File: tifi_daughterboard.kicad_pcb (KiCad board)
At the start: 2 copper layers, 57.4 x 32.3 mm, 19 parts, among them J1 SSW-110-23-F-D, J2 SSW-110-23-F-D, J3 SM04B-SRSS-TB(LF)(SN), J4 SSW-103-02-T-S-RA, Q1 BSS138LT1G, U1 SGP40-D-R4, U2 SHT40-AD1B-R3

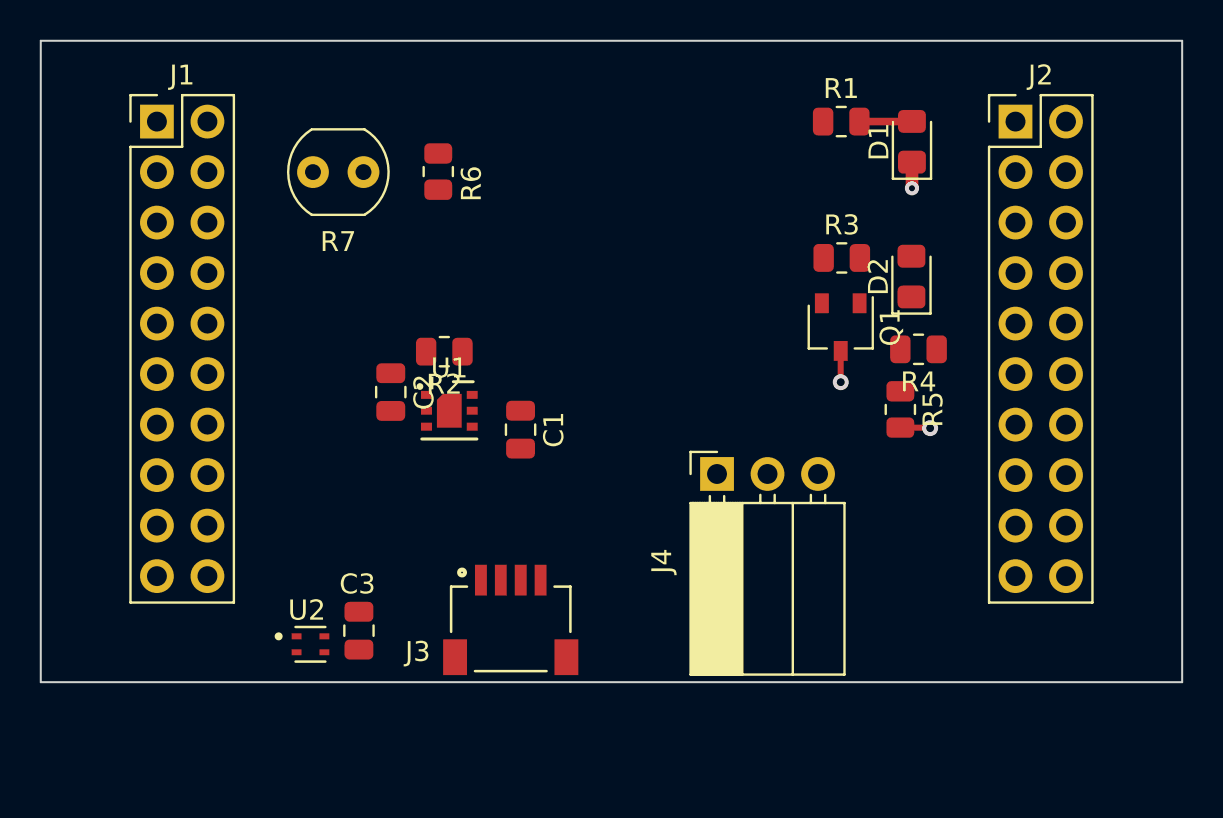
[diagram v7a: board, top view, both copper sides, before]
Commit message: Route I2C connections.
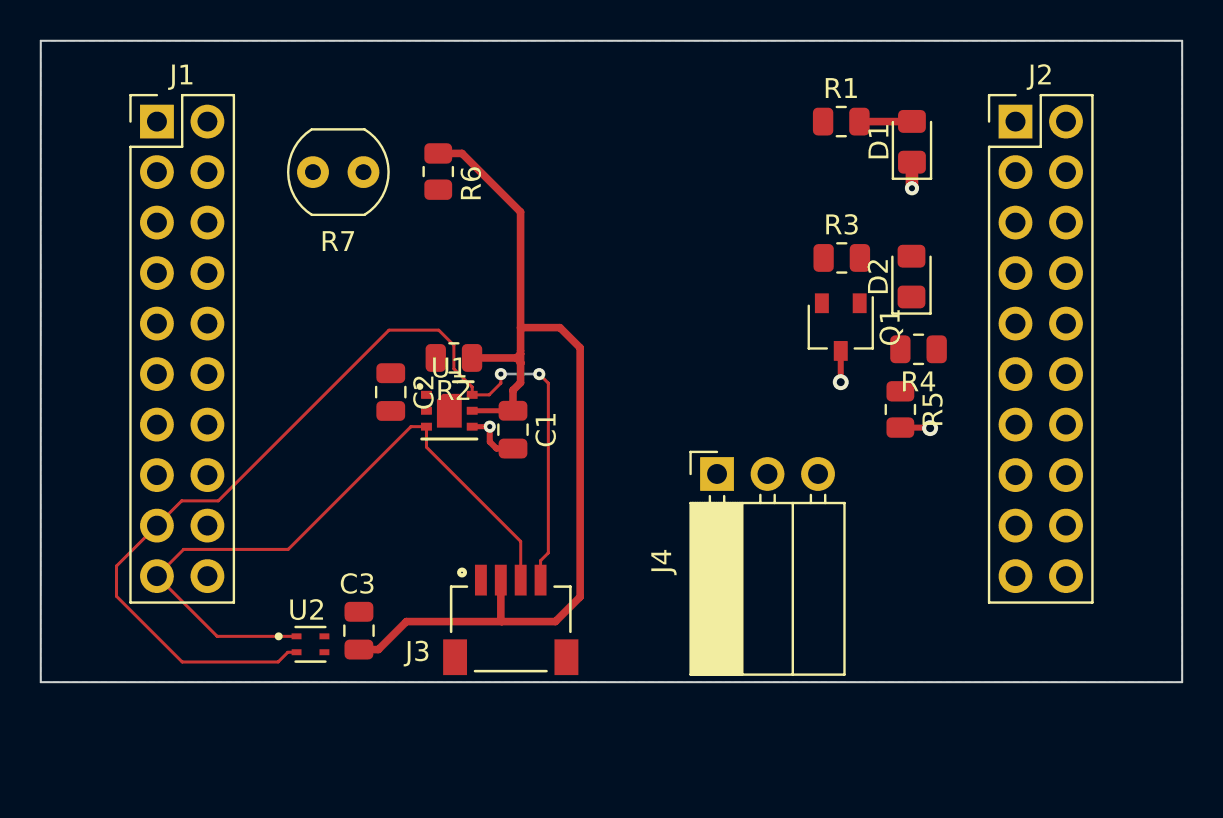
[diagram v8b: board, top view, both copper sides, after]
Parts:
- moved R2 0.58 mm to (136.9, 85.5)
- moved C1 0.38 mm to (139.8, 89.2)
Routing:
- net I2C_SCL: track 0.00 -> 52.0 mm, vias 0 -> 2
- net +3.3V: track 0.00 -> 51.0 mm
- net I2C_SDA: track 0.00 -> 34.6 mm
- net GND: track 4.39 -> 7.35 mm, vias 3 -> 4
- added copper zone on B.Cu, net GND
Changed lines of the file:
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@@
     )
     (pad_to_mask_clearance 0)
+    (grid_origin 140.3858 87.4268)
     (pcbplotparams
       (layerselection 0x00010fc_ffffffff)
@@
   )
   (footprint "Resistor_SMD:R_0805_2012Metric" (layer "F.Cu")
-    (at 136.3726 85.2322 180)
+    (at 136.8552 85.5472 180)
     (descr "Resistor SMD 0805 (2012 Metric), square (rectangular) end terminal, IPC_7351 nominal, (Body size source: IPC-SM-782 page 72, https://www.pcb-3d.com/wordpress/wp-content/uploads/ipc-sm-782a_amendment_1_and_2.pdf), generated with kicad-footprint-generator")
     (tags "resistor")
@@
   )
   (footprint "Capacitor_SMD:C_0805_2012Metric" (layer "F.Cu")
-    (at 140.208 89.154 -90)
+    (at 139.827 89.154 -90)
     (descr "Capacitor SMD 0805 (2012 Metric), square (rectangular) end terminal, IPC_7351 nominal, (Body size source: IPC-SM-782 page 76, https://www.pcb-3d.com/wordpress/wp-content/uploads/ipc-sm-782a_amendment_1_and_2.pdf, https://docs.google.com/spreadsheets/d/1BsfQQcO9C6DZCsRaXUlFlo91Tg2WpOkGARC1WS5S8t0/edit?usp=sharing), generated with kicad-footprint-generator")
     (tags "capacitor")
@@
   )
   (gr_rect (start 116.078 69.596) (end 173.482 101.854) (layer "Edge.Cuts") (width 0.1016) (fill none))
+  (segment (start 139.2682 98.806) (end 134.4676 98.806) (width 0.381) (layer "F.Cu") (net 1))
+  (segment (start 141.9606 98.806) (end 139.2682 98.806) (width 0.381) (layer "F.Cu") (net 1))
+  (segment (start 139.2682 98.806) (end 139.215 98.7528) (width 0.381) (layer "F.Cu") (net 1))
+  (segment (start 136.0678 75.2621) (end 137.2635 75.2621) (width 0.381) (layer "F.Cu") (net 1))
+  (segment (start 139.215 98.7528) (end 139.215 96.7232) (width 0.381) (layer "F.Cu") (net 1))
+  (segment (start 143.2052 97.5614) (end 141.9606 98.806) (width 0.381) (layer "F.Cu") (net 1))
+  (segment (start 133.0604 100.2132) (end 132.08 100.2132) (width 0.381) (layer "F.Cu") (net 1))
+  (segment (start 140.208 78.2066) (end 140.208 84.0232) (width 0.381) (layer "F.Cu") (net 1))
+  (segment (start 140.208 86.7918) (end 139.827 87.1728) (width 0.381) (layer "F.Cu") (net 1))
+  (segment (start 140.208 84.0232) (end 142.1892 84.0232) (width 0.381) (layer "F.Cu") (net 1))
+  (segment (start 140.208 85.852) (end 140.208 85.7504) (width 0.381) (layer "F.Cu") (net 1))
+  (segment (start 139.827 87.1728) (end 139.827 88.204) (width 0.381) (layer "F.Cu") (net 1))
+  (segment (start 142.1892 84.0232) (end 143.2052 85.0392) (width 0.381) (layer "F.Cu") (net 1))
+  (segment (start 140.208 85.344) (end 140.208 85.852) (width 0.381) (layer "F.Cu") (net 1))
+  (segment (start 140.208 85.1916) (end 140.208 85.344) (width 0.381) (layer "F.Cu") (net 1))
+  (segment (start 137.2635 75.2621) (end 140.208 78.2066) (width 0.381) (layer "F.Cu") (net 1))
+  (segment (start 140.208 84.0232) (end 140.208 85.1916) (width 0.381) (layer "F.Cu") (net 1))
+  (segment (start 140.208 85.344) (end 140.0048 85.5472) (width 0.381) (layer "F.Cu") (net 1))
+  (segment (start 143.2052 85.0392) (end 143.2052 97.5614) (width 0.381) (layer "F.Cu") (net 1))
+  (segment (start 137.7766 88.204) (end 139.827 88.204) (width 0.254) (layer "F.Cu") (net 1))
+  (segment (start 140.208 85.852) (end 140.208 86.7918) (width 0.381) (layer "F.Cu") (net 1))
+  (segment (start 137.5645 85.5472) (end 140.0048 85.5472) (width 0.381) (layer "F.Cu") (net 1))
+  (segment (start 134.4676 98.806) (end 133.0604 100.2132) (width 0.381) (layer "F.Cu") (net 1))
+  (segment (start 140.208 85.7504) (end 140.0048 85.5472) (width 0.381) (layer "F.Cu") (net 1))
+  (segment (start 137.7766 89.004) (end 138.6562 89.004) (width 0.254) (layer "F.Cu") (net 2))
+  (segment (start 138.6586 89.7636) (end 138.999 90.104) (width 0.3048) (layer "F.Cu") (net 2))
   (segment (start 159.893 77.0128) (end 159.893 75.701) (width 0.635) (layer "F.Cu") (net 2))
   (segment (start 159.3088 89.0505) (end 160.7801 89.0505) (width 0.3048) (layer "F.Cu") (net 2))
+  (segment (start 138.6562 89.004) (end 138.6586 89.0016) (width 0.254) (layer "F.Cu") (net 2))
   (segment (start 156.3116 85.1959) (end 156.3116 86.7664) (width 0.3048) (layer "F.Cu") (net 2))
+  (segment (start 138.999 90.104) (end 139.827 90.104) (width 0.3048) (layer "F.Cu") (net 2))
   (segment (start 160.7801 89.0505) (end 160.8074 89.0778) (width 0.3048) (layer "F.Cu") (net 2))
+  (segment (start 138.6586 89.0016) (end 138.6586 89.7636) (width 0.3048) (layer "F.Cu") (net 2))
   (via (at 160.8074 89.0778) (size 0.8) (drill 0.4) (layers "F.Cu" "B.Cu") (net 2))
+  (via (at 138.6586 89.0016) (size 0.6096) (drill 0.254) (layers "F.Cu" "B.Cu") (net 2))
   (via (at 159.893 77.0128) (size 0.7112) (drill 0.3048) (layers "F.Cu" "B.Cu") (free) (net 2))
   (via (at 156.3116 86.7664) (size 0.8) (drill 0.4) (layers "F.Cu" "B.Cu") (net 2))
   (segment (start 157.2495 73.66) (end 159.884 73.66) (width 0.381) (layer "F.Cu") (net 3))
   (segment (start 159.884 73.66) (end 159.893 73.651) (width 0.381) (layer "F.Cu") (net 3))
-  (segment (start 135.3585 85.3338) (end 135.5617 85.537) (width 0.508) (layer "F.Cu") (net 43))
+  (segment (start 136.0932 84.1502) (end 133.588785 84.1502) (width 0.1524) (layer "F.Cu") (net 20))
+  (segment (start 136.8552 86.091359) (end 136.8552 84.9122) (width 0.1524) (layer "F.Cu") (net 20))
+  (segment (start 125.003585 92.7354) (end 123.1646 92.7354) (width 0.1524) (layer "F.Cu") (net 20))
+  (segment (start 138.6306 87.404) (end 137.7766 87.404) (width 0.1524) (layer "F.Cu") (net 20))
+  (segment (start 128.505 100.349) (end 128.9416 100.349) (width 0.1524) (layer "F.Cu") (net 20))
+  (segment (start 119.888 97.536) (end 123.19 100.838) (width 0.1524) (layer "F.Cu") (net 20))
+  (segment (start 136.8552 84.9122) (end 136.0932 84.1502) (width 0.1524) (layer "F.Cu") (net 20))
+  (segment (start 139.2174 86.36) (end 139.2174 86.8172) (width 0.1524) (layer "F.Cu") (net 20))
+  (segment (start 121.92 93.98) (end 119.888 96.012) (width 0.1524) (layer "F.Cu") (net 20))
+  (segment (start 141.215 95.7416) (end 141.215 96.7232) (width 0.1524) (layer "F.Cu") (net 20))
+  (segment (start 128.016 100.838) (end 128.505 100.349) (width 0.1524) (layer "F.Cu") (net 20))
+  (segment (start 141.1478 86.36) (end 141.605 86.8172) (width 0.1524) (layer "F.Cu") (net 20))
+  (segment (start 137.7766 87.404) (end 137.7766 87.012759) (width 0.1524) (layer "F.Cu") (net 20))
+  (segment (start 133.588785 84.1502) (end 125.003585 92.7354) (width 0.1524) (layer "F.Cu") (net 20))
+  (segment (start 141.605 86.8172) (end 141.605 95.3516) (width 0.1524) (layer "F.Cu") (net 20))
+  (segment (start 137.7766 87.012759) (end 136.8552 86.091359) (width 0.1524) (layer "F.Cu") (net 20))
+  (segment (start 119.888 96.012) (end 119.888 97.536) (width 0.1524) (layer "F.Cu") (net 20))
+  (segment (start 123.19 100.838) (end 128.016 100.838) (width 0.1524) (layer "F.Cu") (net 20))
+  (segment (start 139.2174 86.8172) (end 138.6306 87.404) (width 0.1524) (layer "F.Cu") (net 20))
+  (segment (start 141.605 95.3516) (end 141.215 95.7416) (width 0.1524) (layer "F.Cu") (net 20))
+  (segment (start 123.1646 92.7354) (end 121.92 93.98) (width 0.1524) (layer "F.Cu") (net 20))
+  (via (at 141.1478 86.36) (size 0.6096) (drill 0.254) (layers "F.Cu" "B.Cu") (net 20))
+  (via (at 139.2174 86.36) (size 0.6096) (drill 0.254) (layers "F.Cu" "B.Cu") (net 20))
+  (segment (start 141.1478 86.36) (end 139.2174 86.36) (width 0.1524) (layer "B.Cu") (net 20))
+  (segment (start 128.521092 95.176708) (end 134.6962 89.0016) (width 0.1524) (layer "F.Cu") (net 22))
+  (segment (start 140.215 94.7744) (end 140.215 96.7232) (width 0.1524) (layer "F.Cu") (net 22))
+  (segment (start 134.6986 89.004) (end 135.4766 89.004) (width 0.1524) (layer "F.Cu") (net 22))
+  (segment (start 135.4766 90.036) (end 140.215 94.7744) (width 0.1524) (layer "F.Cu") (net 22))
+  (segment (start 134.6962 89.0016) (end 134.6986 89.004) (width 0.1524) (layer "F.Cu") (net 22))
+  (segment (start 121.92 96.52) (end 123.263292 95.176708) (width 0.1524) (layer "F.Cu") (net 22))
+  (segment (start 123.263292 95.176708) (end 128.521092 95.176708) (width 0.1524) (layer "F.Cu") (net 22))
+  (segment (start 124.949 99.549) (end 128.9416 99.549) (width 0.1524) (layer "F.Cu") (net 22))
+  (segment (start 135.4766 89.004) (end 135.4766 90.036) (width 0.1524) (layer "F.Cu") (net 22))
+  (segment (start 121.92 96.52) (end 124.949 99.549) (width 0.1524) (layer "F.Cu") (net 22))
+  (zone (net 2) (net_name "GND") (layer "B.Cu") (hatch edge 0.508)
+    (connect_pads (clearance 0.508))
+    (min_thickness 0.254) (filled_areas_thickness no)
+    (fill yes (thermal_gap 0.508) (thermal_bridge_width 0.508))
+    (polygon
+      (pts
+        (xy 173.482 101.854)
+        (xy 116.078 101.854)
+        (xy 116.078 69.596)
+        (xy 173.482 69.596)
+      )
+    )
+  )
 )
